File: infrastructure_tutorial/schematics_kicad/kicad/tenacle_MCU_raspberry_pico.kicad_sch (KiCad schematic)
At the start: 3 parts, among them T201 tentacle_octobus, T202 tentacle_relay

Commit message: Cleanup images
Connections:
- net raspberry rp3/22 / GP17 / RX is gone; now on net raspberry rp3/GP21 / trigger2: T202. (7b)
- net raspberry rp3/26 / GP20 / trigger1 is gone; now on net raspberry rp3/GP21 / trigger2: T202. (7b)
- net raspberry rp3/27 / GP21 / trigger2 is gone; now on net raspberry rp3/GP21 / trigger2: T202. (7b)
- net raspberry rp3/GP21 / trigger2: now reaches T202. (7b)
- net raspberry rp3/19 / GP14 / onewire renamed raspberry rp3/GP14 / onewire
- net raspberry rp3/21 / GP16 / TX renamed raspberry rp3/GP16 / TX
- new net raspberry rp3/GP17 / RX: T202. (7b)
- new net raspberry rp3/GP20 / trigger1: T202. (7b)
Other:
- sheet raspberry rp3 ports: added GP14 / onewire, GP16 / TX, GP17 / RX, GP18 / SDA, GP19 / SCL, GP20 / trigger1, GP21 / trigger2; removed 19 / GP14 / onewire, 21 / GP16 / TX, 22 / GP17 / RX, 24 / GP18 / SDA, 25 / GP19 / SCL, 26 / GP20 / trigger1, 27 / GP21 / trigger2
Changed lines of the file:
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@@
 	(sheet
 		(at 185.42 49.53)
-		(size 40.64 35.56)
+		(size 33.02 36.83)
 		(fields_autoplaced yes)
 		(stroke
@@
 		)
 		(property "Sheetfile" "mcu_raspberry_rp2.kicad_sch"
-			(at 185.42 85.6746 0)
+			(at 185.42 86.9446 0)
 			(effects
 				(font
@@
 			)
 		)
-		(pin "21 {slash} GP16 {slash} TX" input
+		(pin "GP16 {slash} TX" input
 			(at 185.42 68.58 180)
 			(effects
@@
 			)
 		)
-		(pin "26 {slash} GP20 {slash} trigger1" input
+		(pin "GP20 {slash} trigger1" input
 			(at 185.42 58.42 180)
 			(effects
@@
 			)
 		)
-		(pin "27 {slash} GP21 {slash} trigger2" input
+		(pin "GP21 {slash} trigger2" input
 			(at 185.42 63.5 180)
 			(effects
@@
 			)
 		)
-		(pin "22 {slash} GP17 {slash} RX" input
+		(pin "GP17 {slash} RX" input
 			(at 185.42 78.74 180)
 			(effects
@@
 			)
 		)
-		(pin "24 {slash} GP18 {slash} SDA" input
+		(pin "GP18 {slash} SDA" input
 			(at 185.42 81.28 180)
 			(effects
@@
 			)
 		)
-		(pin "25 {slash} GP19 {slash} SCL" input
+		(pin "GP19 {slash} SCL" input
 			(at 185.42 71.12 180)
 			(effects
@@
 			)
 		)
-		(pin "19 {slash} GP14 {slash} onewire" input
+		(pin "GP14 {slash} onewire" input
 			(at 185.42 73.66 180)
 			(effects

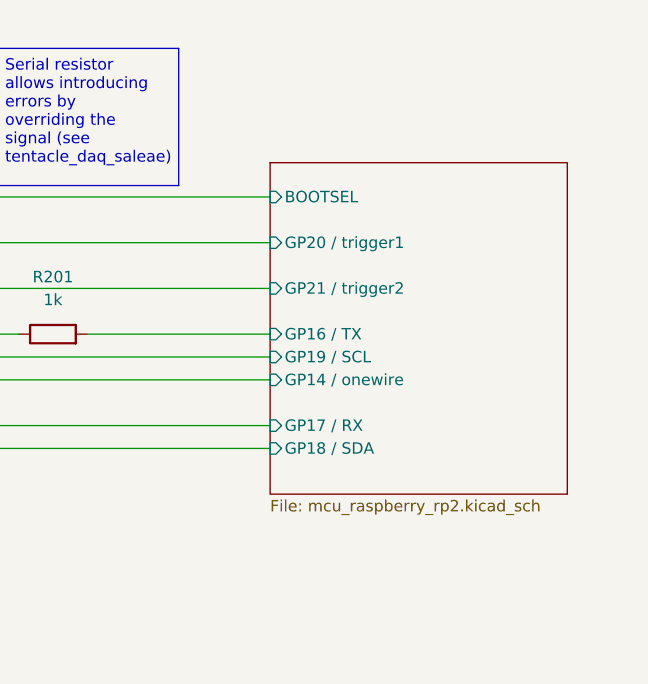
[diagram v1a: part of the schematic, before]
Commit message: Connect pyboard/pico to ground
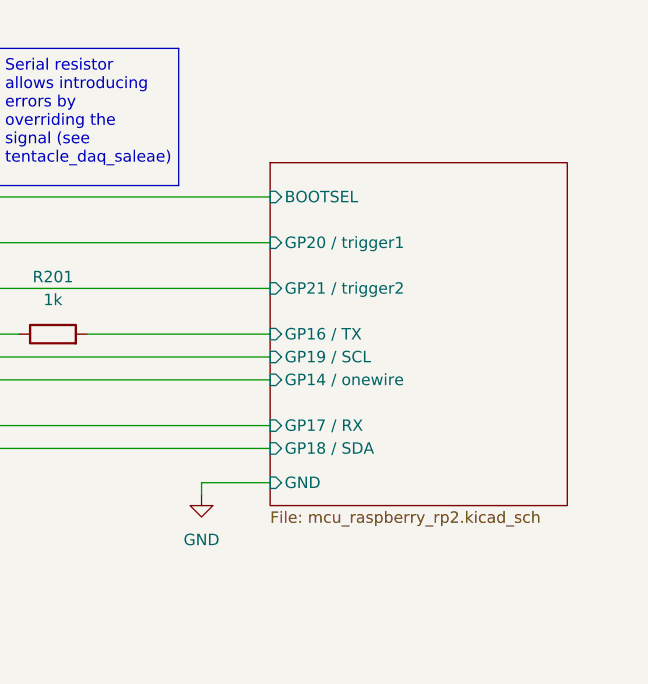
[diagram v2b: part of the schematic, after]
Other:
- sheet raspberry rp3 ports: added GND; removed none
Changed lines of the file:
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@@
+	(wire
+		(pts
+			(xy 177.8 85.09) (xy 177.8 86.36)
+		)
+		(stroke
+			(width 0)
+			(type default)
+		)
+	)
 	(wire
 		(pts
@@
 		(pts
 			(xy 152.4 71.12) (xy 152.4 68.58)
+		)
+		(stroke
+			(width 0)
+			(type default)
+		)
+	)
+	(wire
+		(pts
+			(xy 185.42 85.09) (xy 177.8 85.09)
 		)
 		(stroke
@@
 		)
 	)
+	(symbol
+		(lib_id "power:GND")
+		(at 177.8 86.36 0)
+		(unit 1)
+		(exclude_from_sim no)
+		(in_bom yes)
+		(on_board yes)
+		(dnp no)
+		(fields_autoplaced yes)
+		(property "Reference" "#PWR0203"
+			(at 177.8 92.71 0)
+			(effects
+				(font
+					(size 1.27 1.27)
+				)
+				(hide yes)
+			)
+		)
+		(property "Value" "GND"
+			(at 177.8 91.44 0)
+			(effects
+				(font
+					(size 1.27 1.27)
+				)
+			)
+		)
+		(property "Footprint" ""
+			(at 177.8 86.36 0)
+			(effects
+				(font
+					(size 1.27 1.27)
+				)
+				(hide yes)
+			)
+		)
+		(property "Datasheet" ""
+			(at 177.8 86.36 0)
+			(effects
+				(font
+					(size 1.27 1.27)
+				)
+				(hide yes)
+			)
+		)
+		(property "Description" "Power symbol creates a global label with name \"GND\" , ground"
+			(at 177.8 86.36 0)
+			(effects
+				(font
+					(size 1.27 1.27)
+				)
+				(hide yes)
+			)
+		)
+		(pin "1"
+		)
+		(instances
+			(project "infrastructure"
+				(path "/188054c4-74b7-429a-b3f5-c6f3151e27de/8349ec44-9db3-4e5f-885e-2d604c3fdea6"
+					(reference "#PWR0203")
+					(unit 1)
+				)
+			)
+		)
+	)
 	(sheet
 		(at 185.42 49.53)
-		(size 33.02 36.83)
+		(size 33.02 38.1)
 		(fields_autoplaced yes)
 		(stroke
@@
 		)
 		(property "Sheetfile" "mcu_raspberry_rp2.kicad_sch"
-			(at 185.42 86.9446 0)
+			(at 185.42 88.2146 0)
 			(effects
 				(font
@@
 			(effects
 				(font
+					(size 1.27 1.27)
+				)
+				(justify left)
+			)
+		)
+		(pin "GND" input
+			(at 185.42 85.09 180)
+			(effects
+				(font

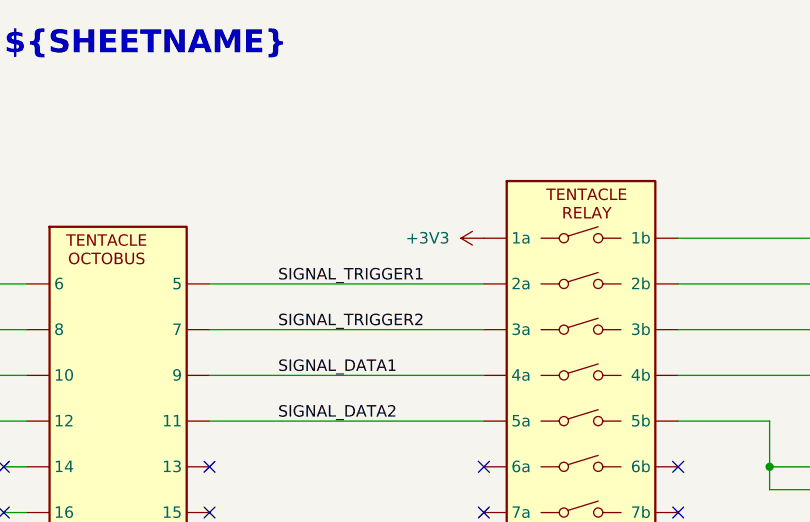
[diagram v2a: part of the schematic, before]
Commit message: pytest for infrastructure_tutorial
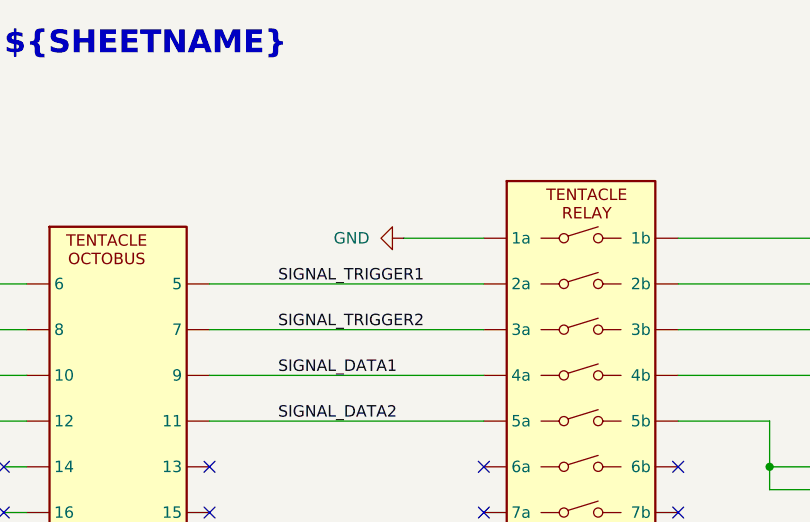
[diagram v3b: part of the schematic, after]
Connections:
- net +3V3 is gone; now on net raspberry rp3/GP21 / trigger2: T202. (7b)
- net GND: now also T202. (7b)
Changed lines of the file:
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@@
+	(wire
+		(pts
+			(xy 105.41 53.34) (xy 114.3 53.34)
+		)
+		(stroke
+			(width 0)
+			(type default)
+		)
+	)
 	(wire
 		(pts
@@
 				(path "/188054c4-74b7-429a-b3f5-c6f3151e27de/8349ec44-9db3-4e5f-885e-2d604c3fdea6"
 					(reference "#PWR0201")
-					(unit 1)
-				)
-			)
-		)
-	)
-	(symbol
-		(lib_id "power:+3V3")
-		(at 114.3 53.34 90)
-		(unit 1)
-		(exclude_from_sim no)
-		(in_bom yes)
-		(on_board yes)
-		(dnp no)
-		(fields_autoplaced yes)
-		(property "Reference" "#PWR0202"
-			(at 118.11 53.34 0)
-			(effects
-				(font
-					(size 1.27 1.27)
-				)
-				(hide yes)
-			)
-		)
-		(property "Value" "+3V3"
-			(at 110.49 53.3399 90)
-			(effects
-				(font
-					(size 1.27 1.27)
-				)
-				(justify left)
-			)
-		)
-		(property "Footprint" ""
-			(at 114.3 53.34 0)
-			(effects
-				(font
-					(size 1.27 1.27)
-				)
-				(hide yes)
-			)
-		)
-		(property "Datasheet" ""
-			(at 114.3 53.34 0)
-			(effects
-				(font
-					(size 1.27 1.27)
-				)
-				(hide yes)
-			)
-		)
-		(property "Description" "Power symbol creates a global label with name \"+3V3\""
-			(at 114.3 53.34 0)
-			(effects
-				(font
-					(size 1.27 1.27)
-				)
-				(hide yes)
-			)
-		)
-		(pin "1"
-		)
-		(instances
-			(project ""
-				(path "/188054c4-74b7-429a-b3f5-c6f3151e27de/8349ec44-9db3-4e5f-885e-2d604c3fdea6"
-					(reference "#PWR0202")
 					(unit 1)
 				)
@@
 					(unit 1)
 				)
+			)
+		)
+	)
+	(symbol
+		(lib_id "power:GND")
+		(at 105.41 53.34 270)
+		(unit 1)
+		(exclude_from_sim no)
+		(in_bom yes)
+		(on_board yes)
+		(dnp no)
+		(fields_autoplaced yes)
+		(property "Reference" "#PWR0204"
+			(at 99.06 53.34 0)
+			(effects
+				(font
+					(size 1.27 1.27)
+				)
+				(hide yes)
+			)
+		)
+		(property "Value" "GND"
+			(at 101.6 53.3399 90)
+			(effects
+				(font
+					(size 1.27 1.27)
+				)
+				(justify right)
+			)
+		)
+		(property "Footprint" ""
+			(at 105.41 53.34 0)
+			(effects
+				(font
+					(size 1.27 1.27)
+				)
+				(hide yes)
+			)
+		)
+		(property "Datasheet" ""
+			(at 105.41 53.34 0)
+			(effects
+				(font
+					(size 1.27 1.27)
+				)
+				(hide yes)
+			)
+		)
+		(property "Description" "Power symbol creates a global label with name \"GND\" , ground"
+			(at 105.41 53.34 0)
+			(effects
+				(font
+					(size 1.27 1.27)
+				)
+				(hide yes)
+			)
+		)
+		(pin "1"
+		)
+		(instances
+			(project "infrastructure"
+				(path "/188054c4-74b7-429a-b3f5-c6f3151e27de/8349ec44-9db3-4e5f-885e-2d604c3fdea6"
+					(reference "#PWR0204")
+					(unit 1)
+				)
